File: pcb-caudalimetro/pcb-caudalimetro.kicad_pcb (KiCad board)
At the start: 2 copper layers, 49 x 70 mm, 24 parts, among them J1 VCC, J2 SNTP_LED, J3 WIFI_LED, J4 FLASH_LED, J6 LAN, J7 PROG, J8 CAUDALIMETRO, SW1 EN, U1 ESP32-WROOM-32, U2 AMS1117-3.3, U3 LM7805_TO220, U4 ULN2003

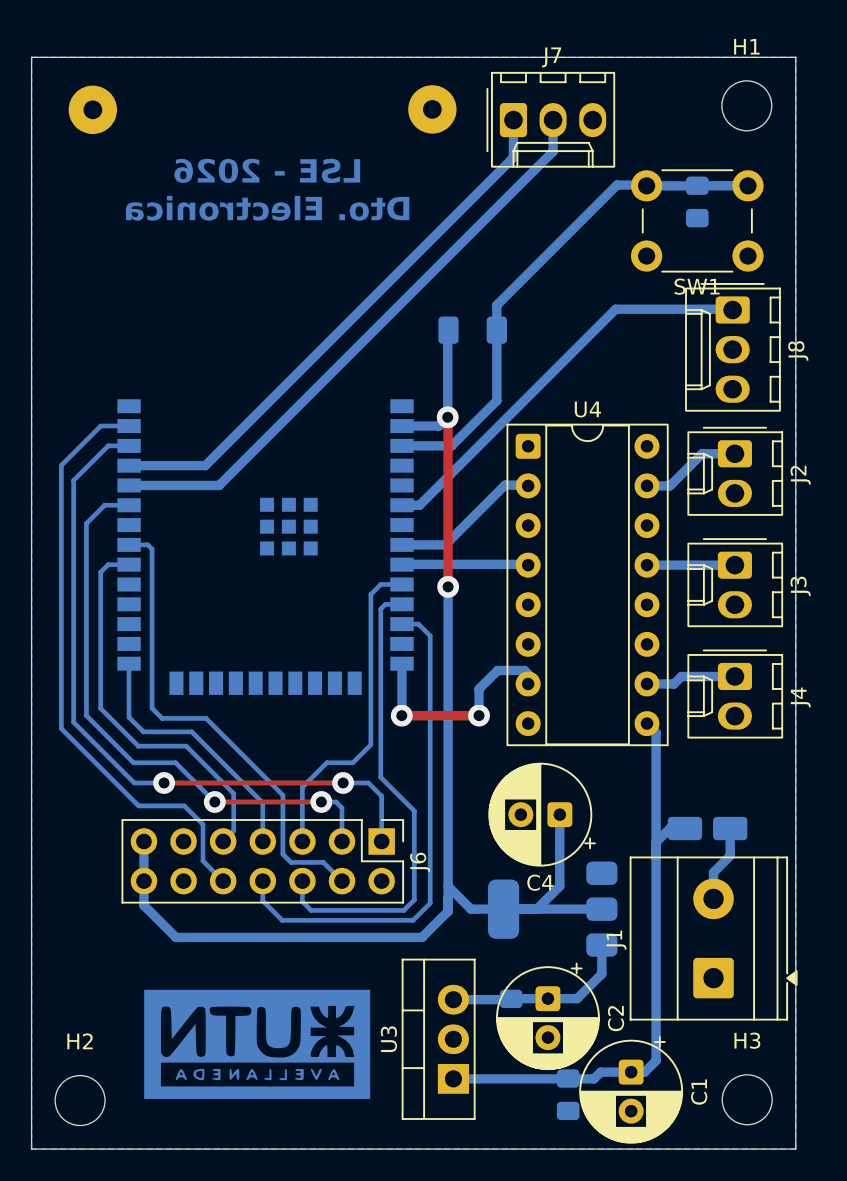
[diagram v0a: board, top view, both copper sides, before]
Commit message: fix: add pull up en gpio input only
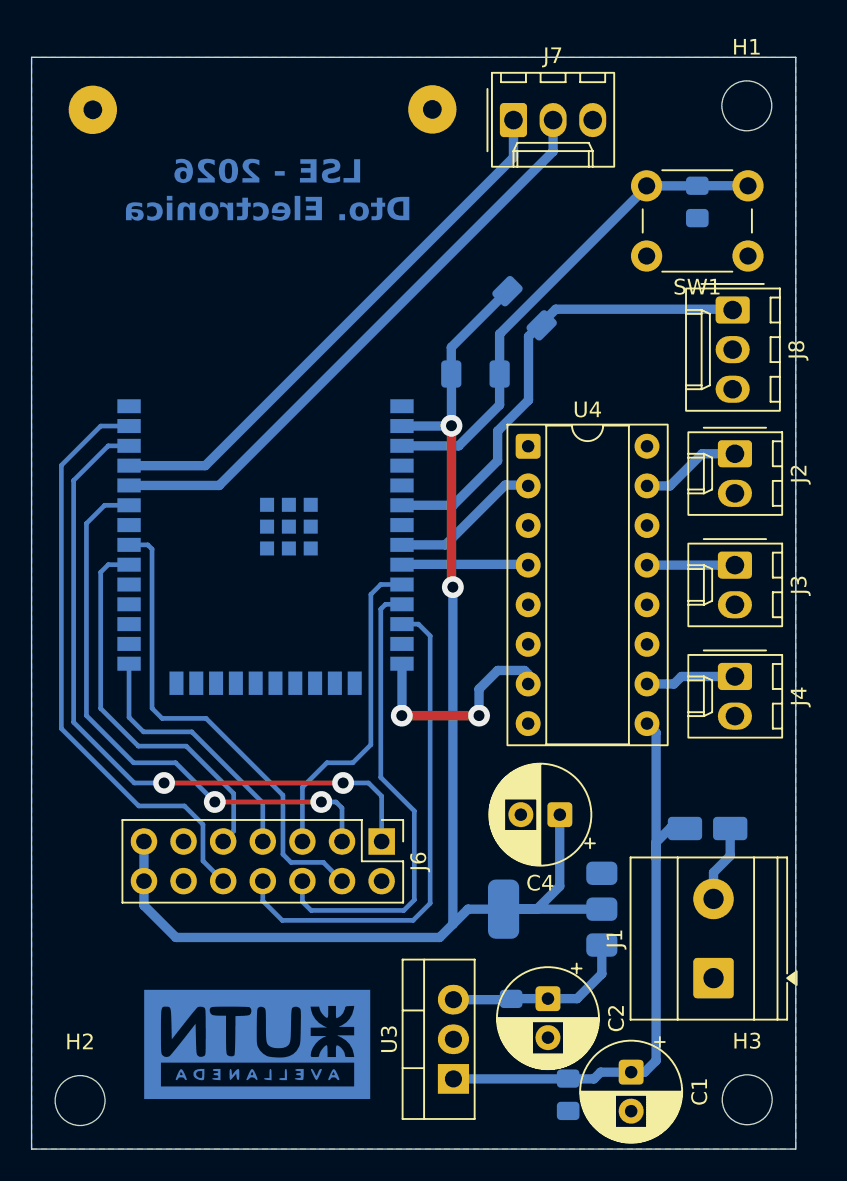
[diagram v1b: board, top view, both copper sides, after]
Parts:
- added R2: 10k, Resistor_SMD:R_1206_3216Metric_Pad1.30x1.75mm_HandSolder, B.Cu at (46.6, 31.1)
- moved R1 2.82 mm to (43.5, 35.3)
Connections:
- J8 pad 2: unconnected-(J8-Pin_2-Pad2) -> GND
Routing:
- net /CAUDALIMETRO: track 26.4 -> 29.9 mm
- net +3V3: track 85.8 -> 89.2 mm
- net /EN: track 33.0 -> 31.8 mm

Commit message: feat: gerbers para grabado laser
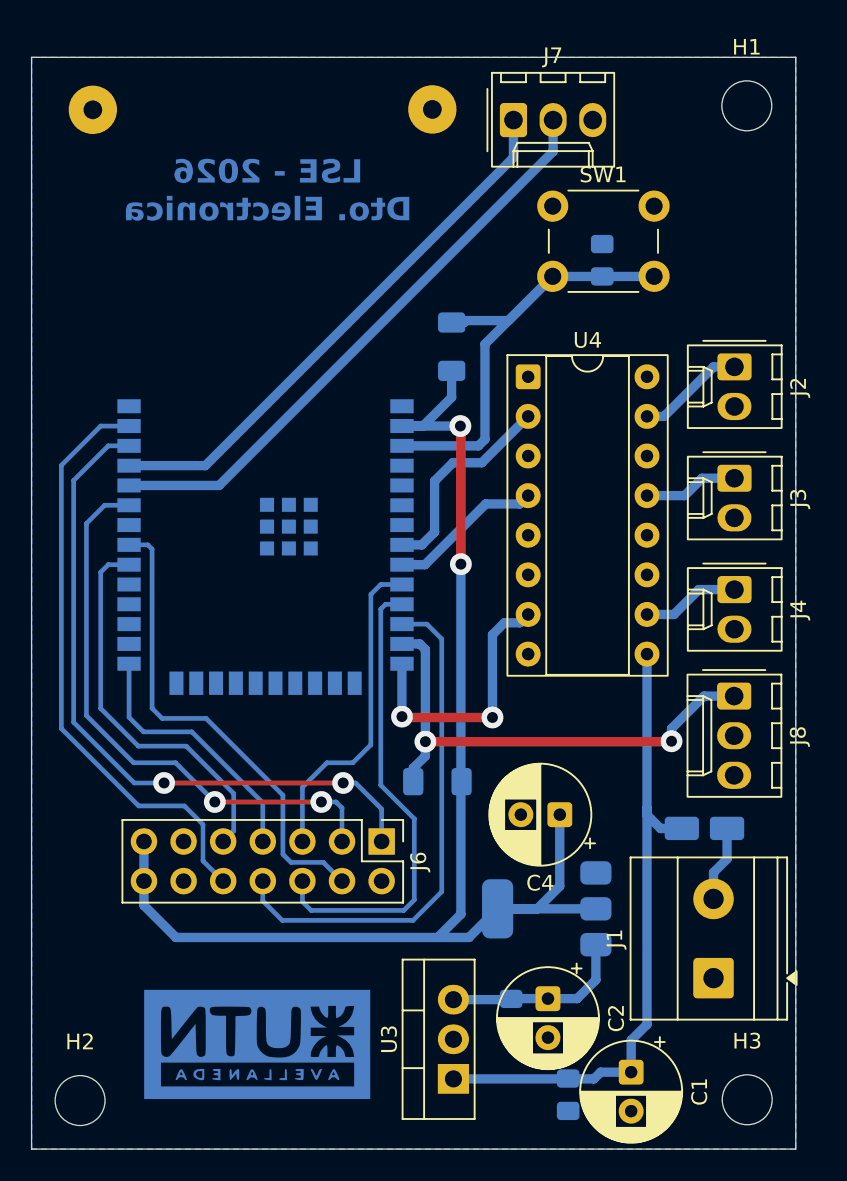
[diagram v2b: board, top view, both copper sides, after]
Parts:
- moved R2 30.9 mm to (41.0, 61.4), turned to 180 degrees
- moved J8 24.8 mm to (60.0, 56.0)
- moved SW1 12.9 mm to (48.4, 24.5), turned to 0 degrees
- moved C7 7.15 mm to (51.6, 28.0), turned to 90 degrees
- moved J2 5.57 mm to (60.1, 34.8)
- moved J3 5.57 mm to (60.1, 42.0)
- moved J4 5.57 mm to (60.1, 49.1)
- moved U4 4.46 mm to (46.8, 35.5)
- moved R1 2.32 mm to (41.9, 33.6), turned to 90 degrees
- moved U2 0.38 mm to (48.0, 69.6)
- moved D1 0.20 mm to (58.1, 64.4)
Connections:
- U1 pad 13: unconnected-(U1-IO14-Pad13) -> /CAUDALIMETRO
- U1 pad 6: /CAUDALIMETRO -> unconnected-(U1-IO34-Pad6)
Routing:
- net /SNTP_ERR: track 9.70 -> 13.4 mm
- net +12V: track 38.6 -> 41.8 mm
- net /FLASH_ERR: track 14.4 -> 17.4 mm
- net /CAUDALIMETRO: track 29.9 -> 31.9 mm, vias 0 -> 2
- net /WIFI_ERR: track 8.12 -> 9.96 mm
- net +3V3: track 89.2 -> 87.5 mm
- net /CRS: track 32.2 -> 33.2 mm

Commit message: chore: generar gerbers y BOM
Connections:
- U4 pad 11: GND -> unconnected-(U4-O6-Pad11)
- U4 pad 12: GND -> unconnected-(U4-O5-Pad12)
- U4 pad 14: GND -> unconnected-(U4-O3-Pad14)
- U4 pad 16: GND -> unconnected-(U4-O1-Pad16)
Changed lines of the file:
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@@
 			(layers "*.Cu" "*.Mask")
 			(remove_unused_layers no)
-			(net "GND")
+			(net "unconnected-(U4-O6-Pad11)")
 			(pinfunction "O6_11")
 			(pintype "open_collector")
@@
 			(layers "*.Cu" "*.Mask")
 			(remove_unused_layers no)
-			(net "GND")
+			(net "unconnected-(U4-O5-Pad12)")
 			(pinfunction "O5_12")
 			(pintype "open_collector")
@@
 			(layers "*.Cu" "*.Mask")
 			(remove_unused_layers no)
-			(net "GND")
+			(net "unconnected-(U4-O3-Pad14)")
 			(pinfunction "O3_14")
 			(pintype "open_collector")
@@
 			(layers "*.Cu" "*.Mask")
 			(remove_unused_layers no)
-			(net "GND")
+			(net "unconnected-(U4-O1-Pad16)")
 			(pinfunction "O1_16")
 			(pintype "open_collector")
